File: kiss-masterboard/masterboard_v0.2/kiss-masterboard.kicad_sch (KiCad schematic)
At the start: 31 parts, among them J1 Cubebatt_host, J17 Conn_02x05_Counter_Clockwise, J18 Conn_02x02_Counter_Clockwise, J19 Conn_01x07, J2 Conn_01x02, J3 Conn_01x02, J4 Conn_01x02, J5 Conn_01x02, J6 Conn_01x02, J7 Conn_01x02

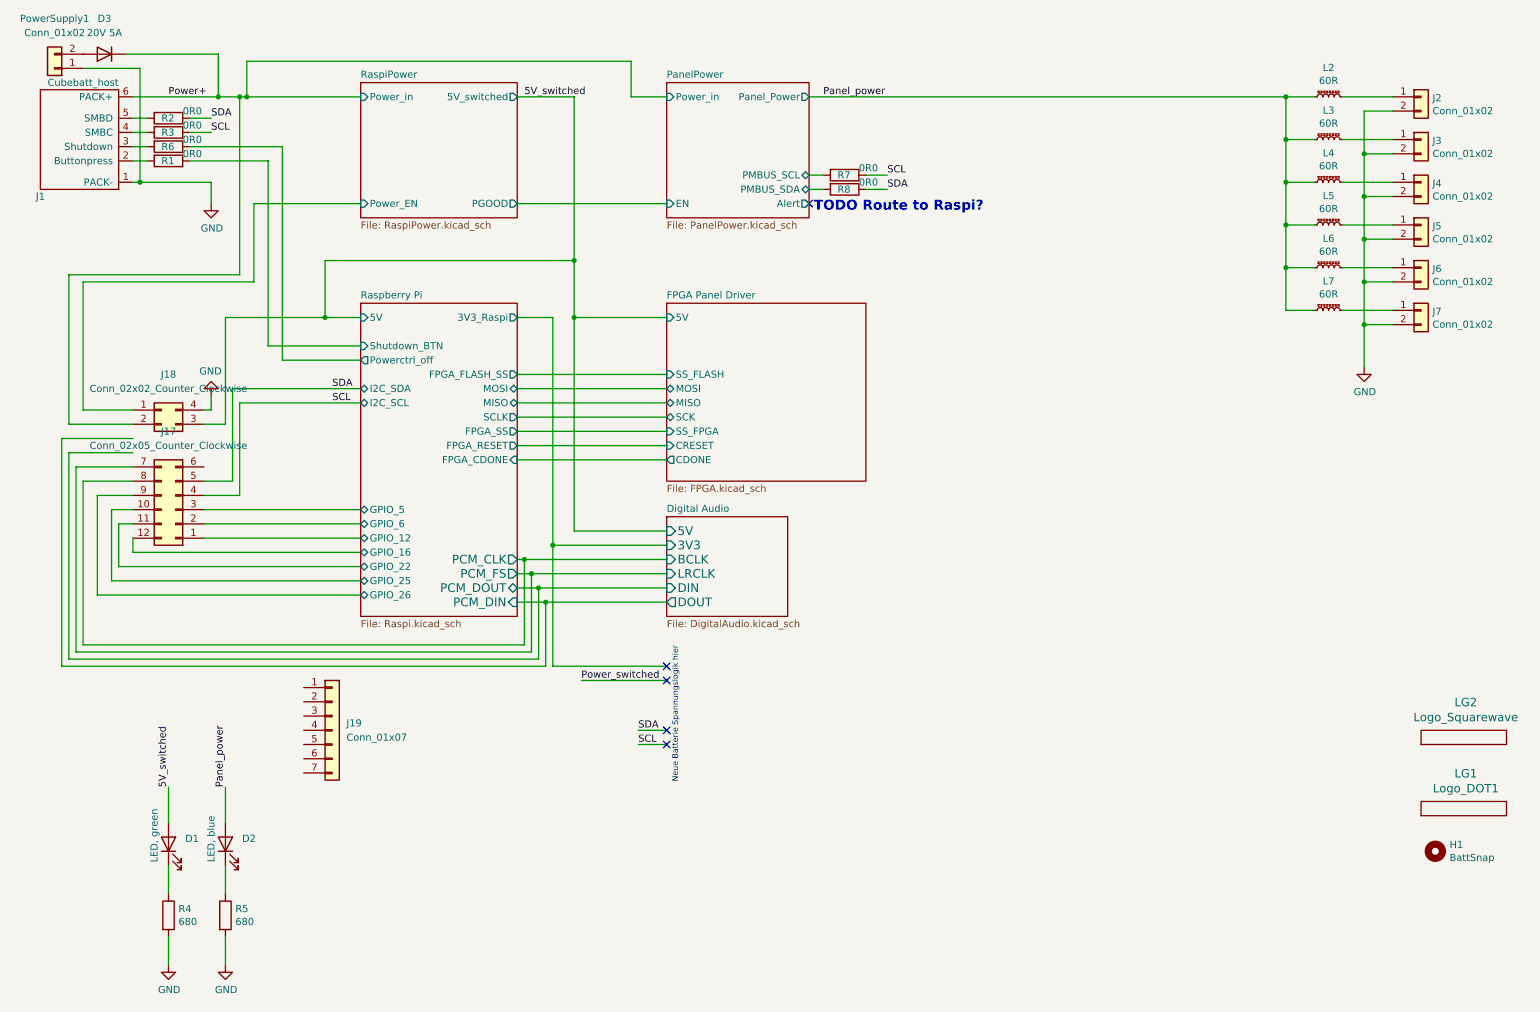
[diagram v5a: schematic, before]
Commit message: Added IMU, routed extension layer, switched battery polarity
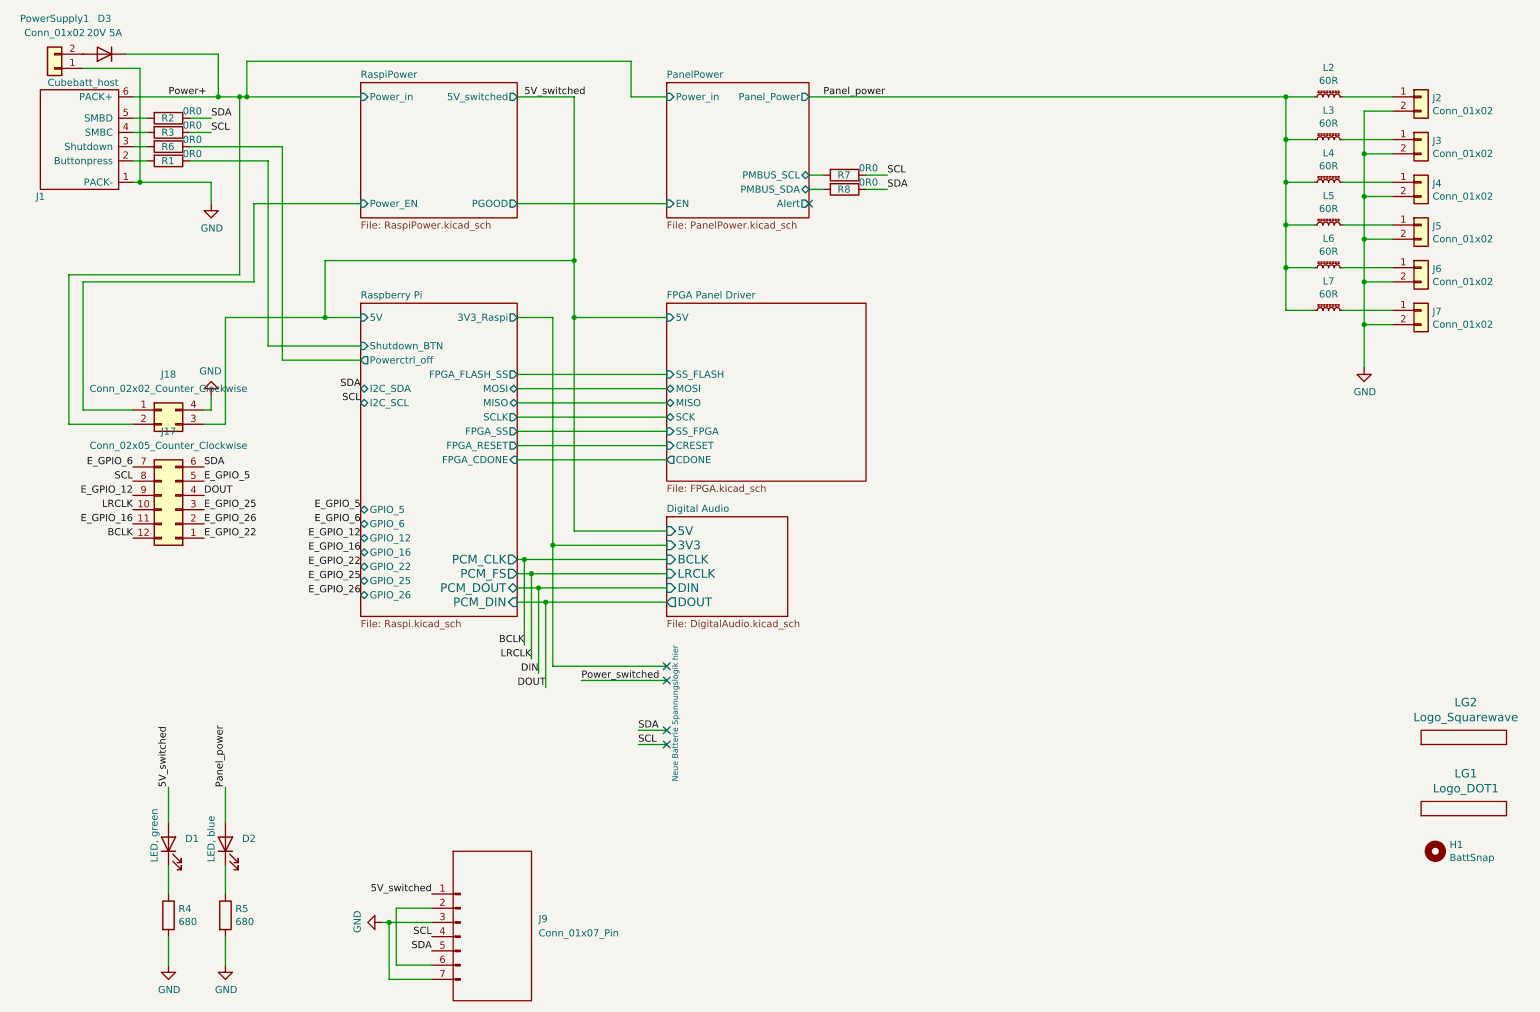
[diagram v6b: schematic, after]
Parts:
- removed J19: Conn_01x07, symbol Connector_Generic:Conn_01x07
- added J9: Conn_01x07_Pin, kiss:PinHeader_1x07_imu, symbol kiss:IMU
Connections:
- net Digital Audio/BCLK is gone; now on net SCL: J17.8 (Pin_8)
- net 5V_switched: now also J9.1 (Pin_1)
- net GND: now also J9.3 (Pin_3), J9.7 (Pin_7)
- net SCL: now also J9.4 (Pin_4); no longer J17.4 (Pin_4)
- net SDA: now also J17.6 (Pin_6), J9.5 (Pin_5); no longer J17.5 (Pin_5)
- net Digital Audio/LRCLK renamed E_GPIO_6
- net Raspberry Pi/GPIO_12 renamed E_GPIO_22
- net Raspberry Pi/GPIO_16 renamed BCLK
- net Raspberry Pi/GPIO_22 renamed E_GPIO_16
- net Raspberry Pi/GPIO_25 renamed LRCLK
- net Raspberry Pi/GPIO_26 renamed E_GPIO_12
- net Raspberry Pi/GPIO_5 renamed E_GPIO_25
- net Raspberry Pi/GPIO_6 renamed E_GPIO_26
- new net: J9.2 (Pin_2), J9.6 (Pin_6)
- new net DOUT: J17.4 (Pin_4)
- new net E_GPIO_5: J17.5 (Pin_5)
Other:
- note removed: "TODO Route to Raspi?"

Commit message: add cnumbers initial order v04a
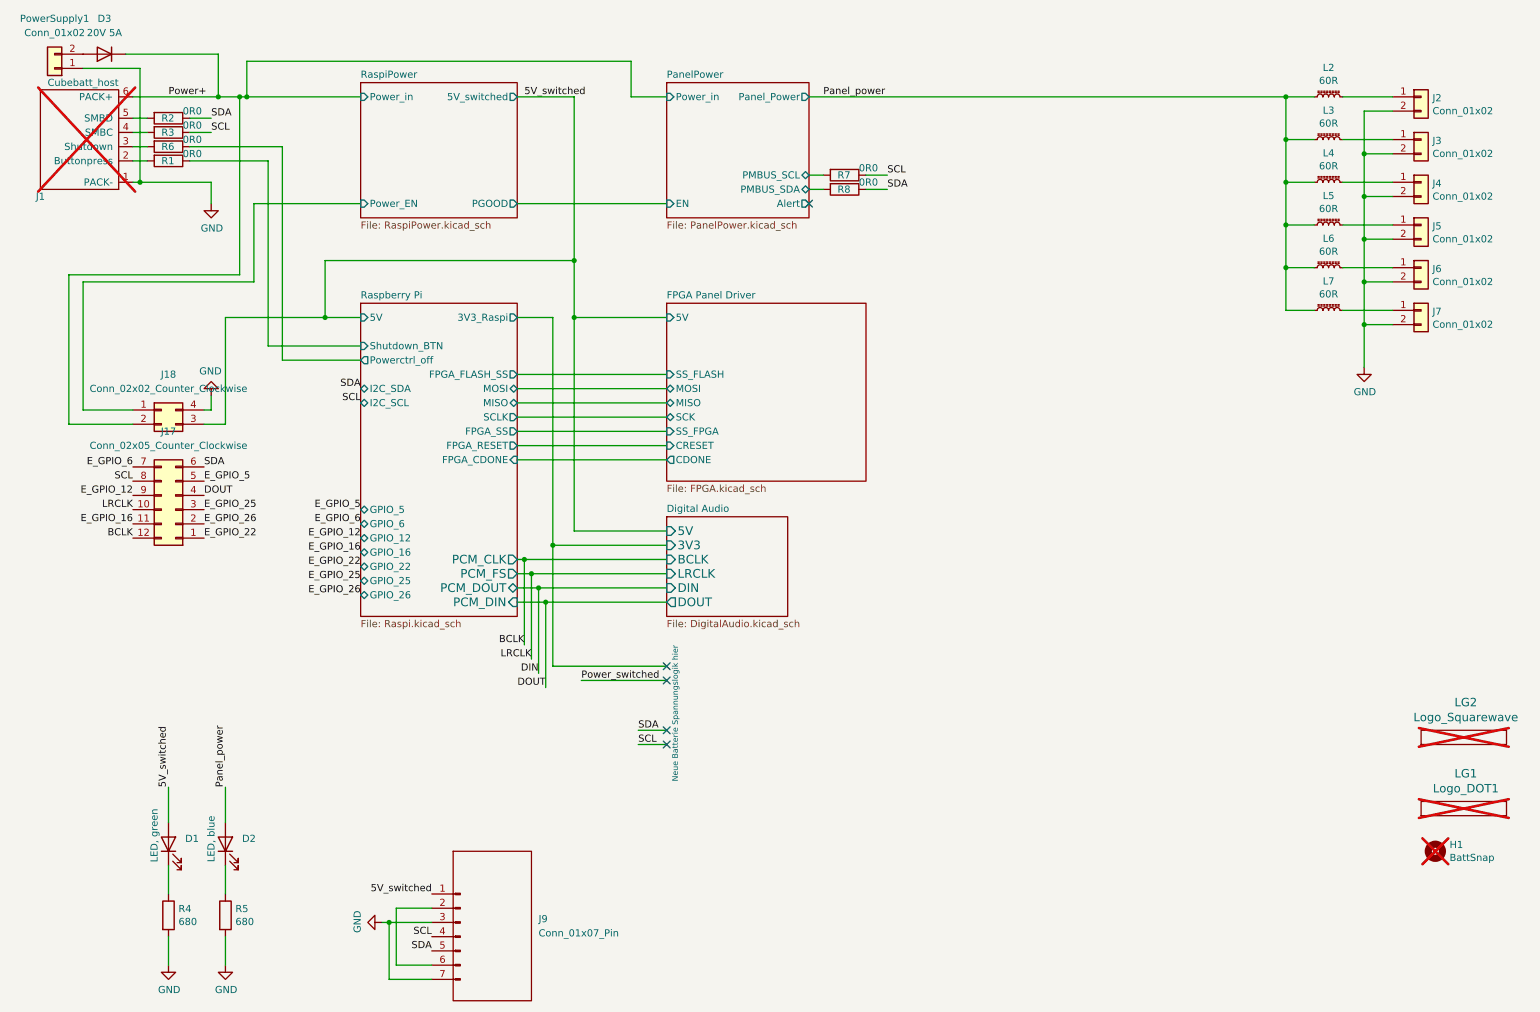
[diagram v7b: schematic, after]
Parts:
- D1: JLCNR (none) -> C2290
- D2: JLCNR (none) -> C2286
- D3: JLCNR (none) -> C5818966
- H1, J1, LG1, LG2: now not fitted
- J17: JLCNR (none) -> C32713285
- J18: JLCNR (none) -> C919361
- L2, L3, L4, L5, L6, L7: JLCNR (none) -> C48543410
- R1, R2, R3, R6, R7, R8: JLCNR (none) -> C21189
- R4, R5: JLCNR (none) -> C23228
